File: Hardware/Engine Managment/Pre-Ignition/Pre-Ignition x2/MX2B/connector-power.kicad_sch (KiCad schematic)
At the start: 13 parts, among them IC1 L78M05ABDT-TR, J2 Conn_01x04, J3 Conn_01x04, J4 Conn_02x12_Counter_Clockwise, J5 Conn_01x04, J7 Conn_01x04

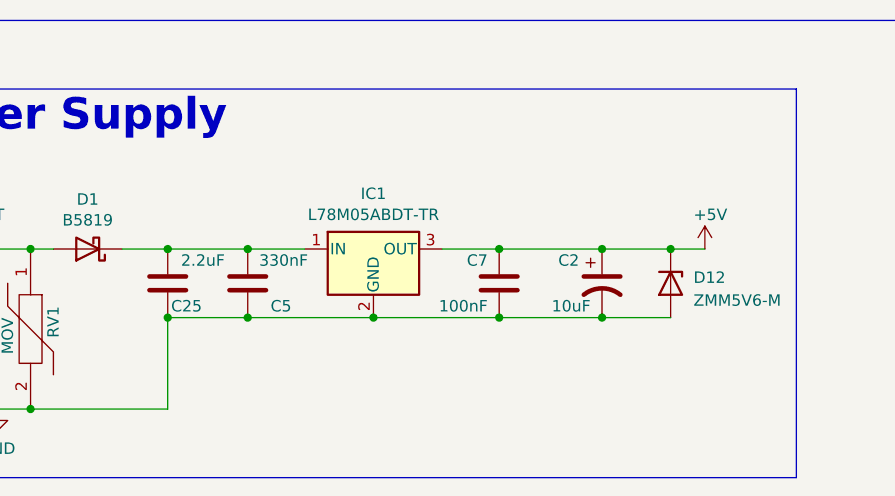
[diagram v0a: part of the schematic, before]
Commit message: schematic exports
kicad version updates, schematic exports
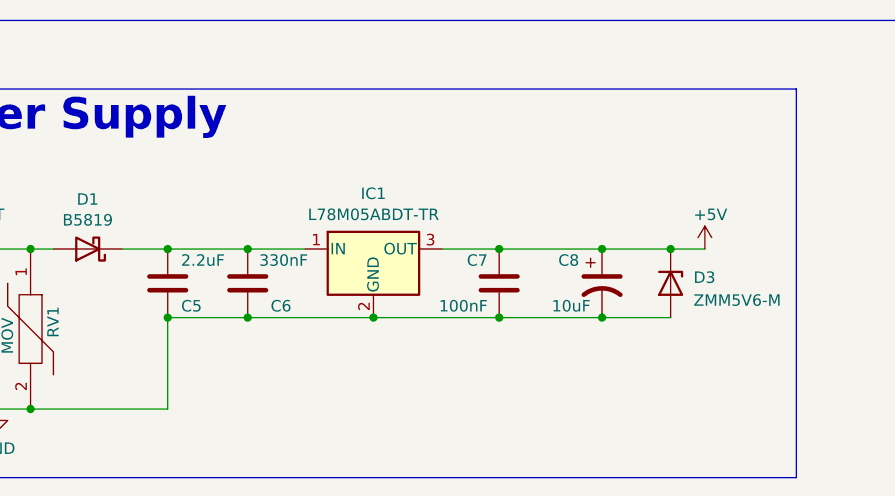
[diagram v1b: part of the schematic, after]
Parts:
- renumbered C25 to C5, C5 to C6, C2 to C8, D12 to D3
